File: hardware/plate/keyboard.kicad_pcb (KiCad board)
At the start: 2 copper layers, 390 x 247.8 mm, 331 parts, among them J1 USB_C_Receptacle_USB2.0, J2 SWD, Q1 BSS138, Q2 BSS138, Q3 DTC123J, SW1 SW_Push, U1 USBLC6-2SC6, U2 AP2112K-3.3, U3 STM32F303RCTx, Y1 8MHz

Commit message: update mounting hole locations
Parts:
- removed BZ1: Buzzer, Buzzer_Beeper:Buzzer_Murata_PKMCS0909E4000-R1
- removed C1, C2: 1u, Capacitor_SMD:C_0603_1608Metric
- removed C10, C11, C12, C13, C14, C15, C16, C17, C18, C19, C20, C21, C22, C23, C24, C25, C27, C28, C29, C30, C32, C33, C34, C35, C36, C37, C38, C39, C6, C7, C8, C9: 100n, Capacitor_SMD:C_0603_1608Metric
- removed C26: 4u7, Capacitor_SMD:C_0603_1608Metric
- removed C3, C40: 10u, Capacitor_SMD:C_0603_1608Metric
- removed C4, C5: 22P, Capacitor_SMD:C_0603_1608Metric
- removed D1, D10, D11, D12, D13, D15, D17, D2, D20, D3, D4, D5, D6, D7, D8, D9: WS2812B, LED_SMD:LED_WS2812B_PLCC4_5.0x5.0mm_P3.2mm
- removed D14: LED, LED_SMD:LED_0603_1608Metric
- removed D21, D22, D23, D25: SK6812-MINI-E, josh-led:SK8612-MINI-E
- removed D24, D_0, D_1, D_10, D_100, D_101, D_102, D_103, D_104, D_105, D_106, D_107, D_108, D_11, D_110, D_112, D_114, D_12, D_13, D_14, D_15, D_16, D_17, D_18, D_19, D_2, D_20, D_21, D_22, D_23, D_24, D_25, D_26, D_27, D_28, D_29, D_3, D_30, D_31, D_32, D_33, D_34, D_35, D_36, D_37, D_38, D_39, D_4, D_40, D_41, D_42, D_43, D_44, D_45, D_46, D_47, D_48, D_49, D_5, D_50, D_51, D_52, D_53, D_54, D_55, D_56, D_57, D_58, D_6, D_60, D_61, D_62, D_63, D_64, D_65, D_66, D_67, D_68, D_69, D_7, D_70, D_71, D_72, D_73, D_74, D_75, D_76, D_77, D_78, D_79, D_8, D_80, D_81, D_82, D_83, D_84, D_85, D_86, D_87, D_88, D_89, D_9, D_90, D_91, D_92, D_93, D_94, D_95, D_97, D_98, D_99: 1N4148, Diode_SMD:D_SOD-123
- removed F1: 500mA, josh-passives-smt:Fuse_0805_2012Metric
- removed FB1, FB2: 600R, josh-passives-smt:Ferrite_Bead_0603
- removed J1: USB_C_Receptacle_USB2.0, josh-connectors:USB_C_U262-161N-4BVC11
- removed J2: SWD, josh-connectors:STM_4_PIN_THT_Staggered
- removed K_0, K_1, K_2, K_3: Encoder_MX, josh-keyboard:MX_KEYSWITCH_ENCODER
- removed K_10, K_105, K_106, K_107, K_108, K_109, K_11, K_113, K_114, K_115, K_12, K_13, K_14, K_15, K_16, K_17, K_18, K_19, K_20, K_21, K_22, K_23, K_24, K_25, K_26, K_27, K_28, K_29, K_30, K_31, K_32, K_33, K_34, K_35, K_36, K_38, K_39, K_4, K_41, K_42, K_43, K_45, K_46, K_47, K_48, K_49, K_5, K_50, K_51, K_52, K_53, K_54, K_55, K_56, K_58, K_59, K_6, K_60, K_61, K_62, K_64, K_65, K_66, K_67, K_68, K_69, K_7, K_70, K_71, K_72, K_73, K_74, K_76, K_77, K_79, K_8, K_80, K_81, K_83, K_84, K_85, K_86, K_87, K_88, K_89, K_9, K_90, K_91, K_92, K_94, K_95, K_96, K_97: KEYSW, josh-keyboard:MXOnly-1U-NoLED
- removed K_100, K_101, K_111, K_99: KEYSW, josh-keyboard:MXOnly-1.25U-NoLED
- removed K_102: KEYSW, josh-keyboard:MXOnly-6.25U-ReversedStabilizers-NoLED
- removed K_103, K_104, K_44, K_57: KEYSW, josh-keyboard:MXOnly-1.5U-NoLED
- removed K_110: KEYSW, josh-keyboard:MXOnly-2.75U-ReversedStabilizers-NoLED
- removed K_112, K_75, K_82: KEYSW, josh-keyboard:MXOnly-2.25U-ReversedStabilizers-NoLED
- removed K_37, K_40, K_78: KEYSW, josh-keyboard:MXOnly-2U-NoLED
- removed K_63, K_93: KEYSW, josh-keyboard:MXOnly-1.75U-NoLED
- removed K_98: KEYSW, josh-keyboard:MXOnly-2U-ReversedStabilizers-NoLED
- removed Q1, Q2: BSS138, Package_TO_SOT_SMD:SOT-23
- removed Q3: DTC123J, Package_TO_SOT_SMD:SOT-23
- removed R1, R2, R3, R4: 10K, Resistor_SMD:R_0603_1608Metric
- removed R10, R11, R7, R9: 1K5, Resistor_SMD:R_0603_1608Metric
- removed R5, R6: 5K1, Resistor_SMD:R_0603_1608Metric
- removed R8: 100K, Resistor_SMD:R_0603_1608Metric
- removed RN1, RN2, RN3, RN4: 10K, Resistor_SMD:R_Array_Convex_4x0603
- removed SW1: SW_Push, josh-buttons-switches:Panasonic_EVQPUL_EVQPUC
- removed U1: USBLC6-2SC6, Package_TO_SOT_SMD:SOT-23-6
- removed U2: AP2112K-3.3, Package_TO_SOT_SMD:SOT-23-5
- removed U3: STM32F303RCTx, Package_QFP:LQFP-64_10x10mm_P0.5mm
- removed Y1: 8MHz, josh-oscillators:Crystal_SMD_3225-4Pin_3.2x2.5mm
- H1, H10, H11, H12, H2, H3, H4, H5, H6, H7, H8, H9: value 3.5mm ID -> M2.5; footprint MountingHole:MountingHole_3.5mm -> MountingHole:MountingHole_2.7mm_M2.5
- moved LOGO3 229.4 mm to (412.8, 185.4), turned to 270 degrees
- moved LOGO2 217.3 mm to (413.5, 170.9), turned to 270 degrees
- moved LOGO1 216.4 mm to (409.8, 174.6), turned to 270 degrees
- moved H9 0.51 mm to (157.1, 109.5)
- moved H4 0.40 mm to (461.6, 128.5)
- moved H10 0.30 mm to (138.0, 185.7)
- moved H1 0.20 mm to (119.0, 166.7)
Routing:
- net +5V: track 1088.2 -> 0.00 mm, vias 10 -> 0
- net /row5: track 440.0 -> 0.00 mm, vias 10 -> 0
- net /row0: track 403.8 -> 0.00 mm, vias 4 -> 0
- net /col19: track 402.2 -> 0.00 mm, vias 1 -> 0
- net /row1: track 383.4 -> 0.00 mm, vias 4 -> 0
- net /col18: track 381.3 -> 0.00 mm, vias 1 -> 0
- net /row4: track 378.9 -> 0.00 mm, vias 4 -> 0
- net /col17: track 378.8 -> 0.00 mm, vias 1 -> 0
- net /row3: track 362.9 -> 0.00 mm, vias 3 -> 0
- net +3V3: track 360.6 -> 0.00 mm, vias 15 -> 0
- net /row2: track 358.8 -> 0.00 mm, vias 5 -> 0
- net /col16: track 344.9 -> 0.00 mm, vias 1 -> 0
- net /col15: track 322.0 -> 0.00 mm, vias 1 -> 0
- net /col14: track 304.7 -> 0.00 mm, vias 1 -> 0
- net /col13: track 262.3 -> 0.00 mm, vias 1 -> 0
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- removed copper zone on B.Cu, net GND
- removed copper zone on F.Cu, net GND
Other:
- board size 390 x 247.8 mm -> 390 x 120.2 mm
- board text removed: "GND"
- board text removed: "PWR"
- board text removed: "RST"
- board text removed: "SWDCLK"
- board text removed: "SWDIO"
- board text removed: "nRST"

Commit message: mechanical changes
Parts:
- H1, H10, H11, H12, H2, H3, H4, H5, H6, H7, H8, H9: footprint MountingHole:MountingHole_2.7mm_M2.5 -> MountingHole:MountingHole_2.2mm_M2
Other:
- outline, holes or cut-outs redrawn

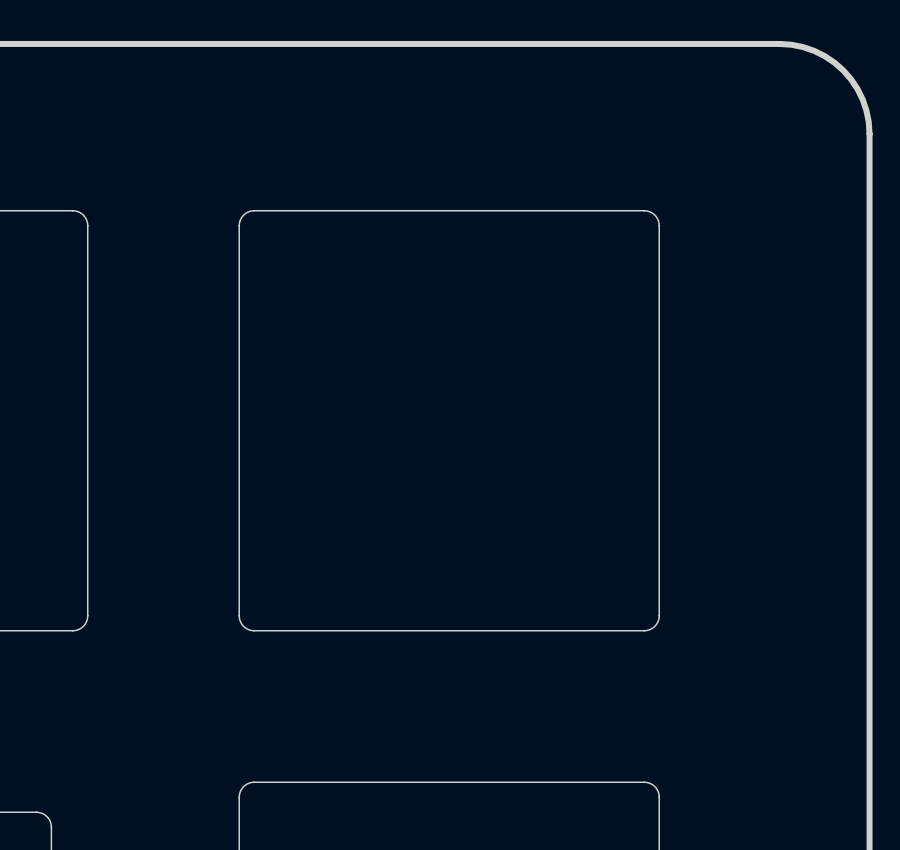
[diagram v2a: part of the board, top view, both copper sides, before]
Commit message: add encoder top right
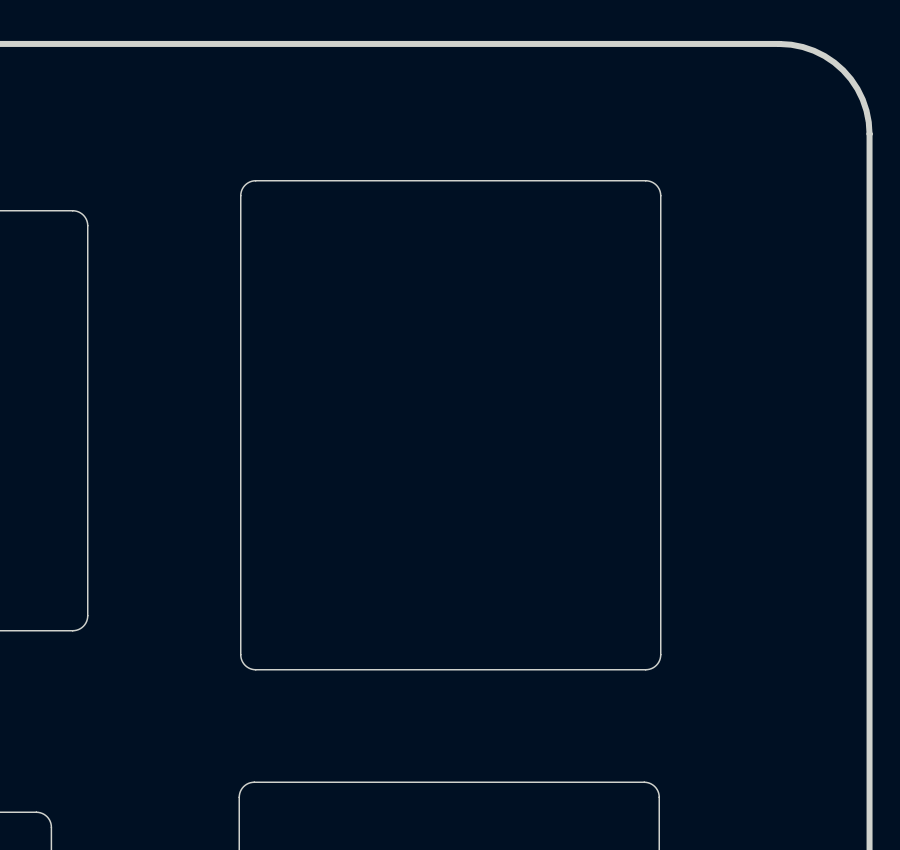
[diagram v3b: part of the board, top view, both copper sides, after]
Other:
- outline, holes or cut-outs redrawn

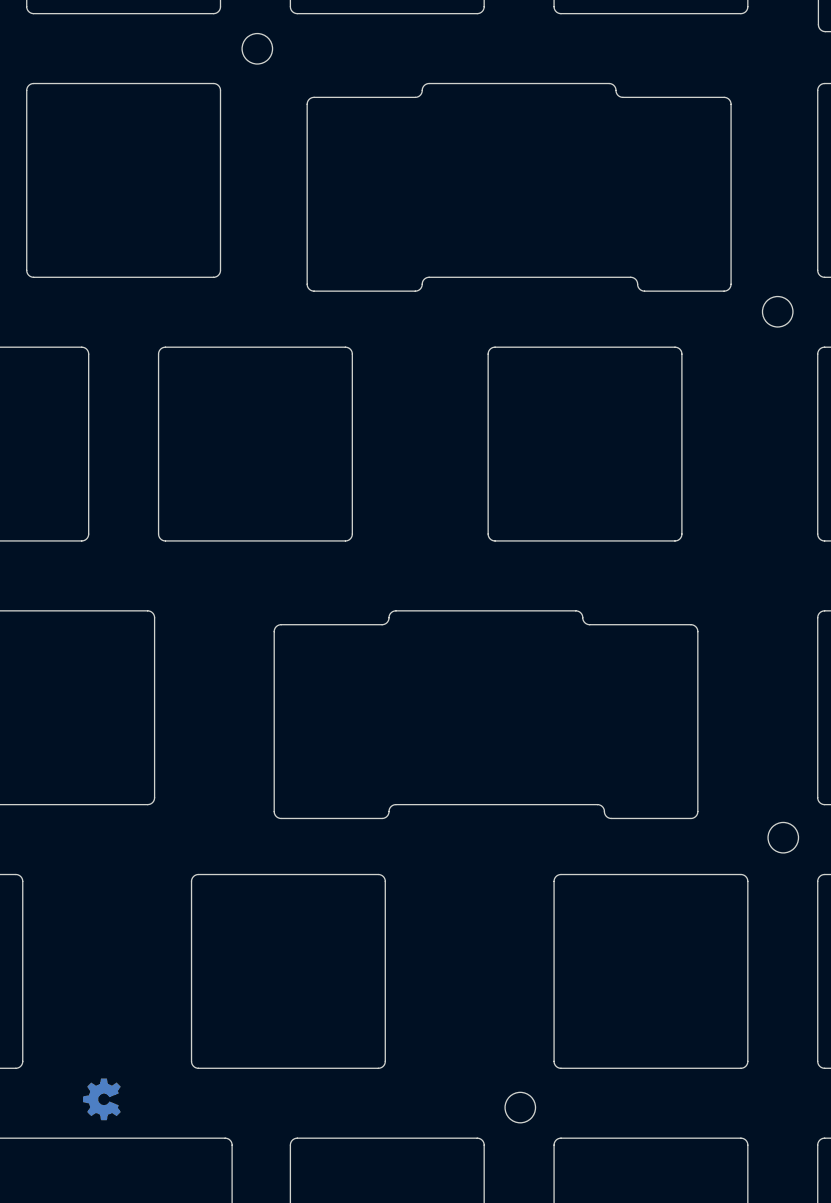
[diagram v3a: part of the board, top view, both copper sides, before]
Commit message: add split backspace
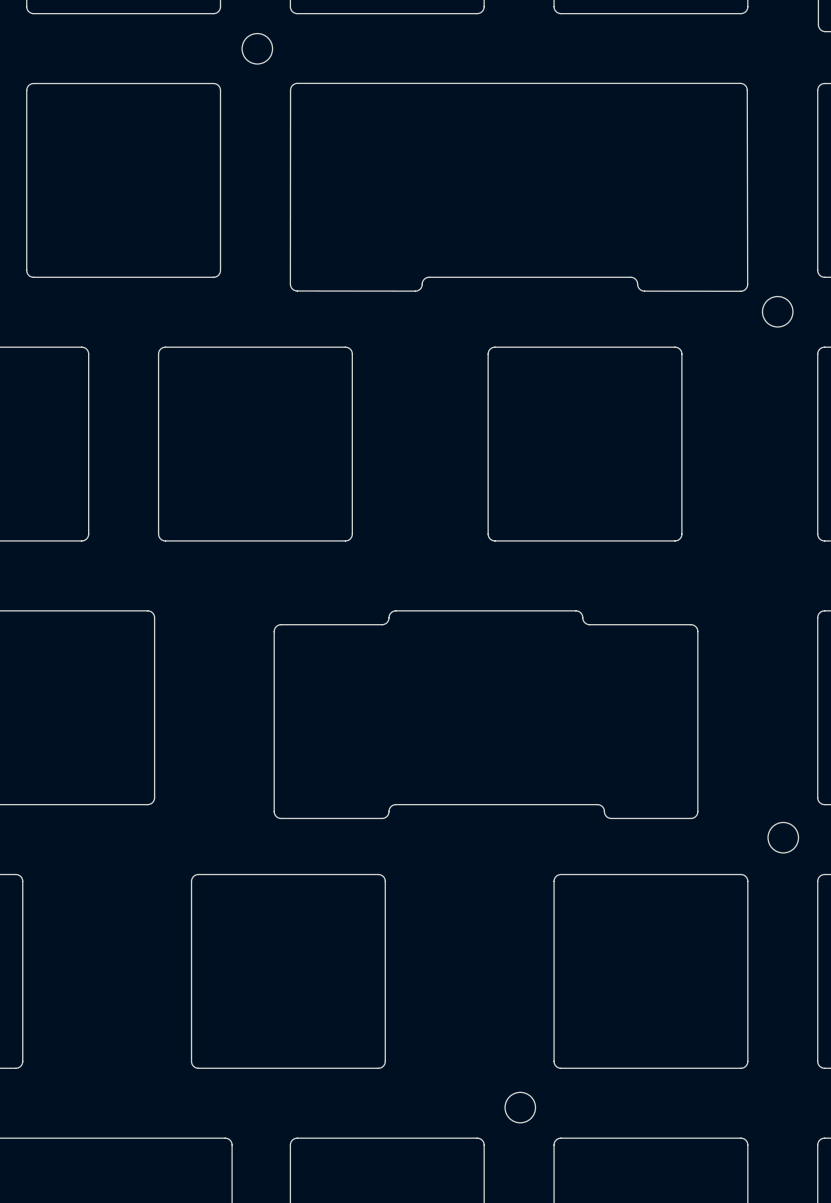
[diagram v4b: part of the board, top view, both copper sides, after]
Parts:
- removed LOGO1: Josh-Logo, josh-logos:josh-johnson-logo-17x3
- removed LOGO2: Josh-Details, josh-logos:josh-details
- removed LOGO3: OSHW Logo, josh-logos:OSHW_Logo_3.6x3.6_F.Mask
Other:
- outline, holes or cut-outs redrawn
